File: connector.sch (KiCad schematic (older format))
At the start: 1 part, among them J11 DB15_Female_HighDensity_Mount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

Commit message: Added connector
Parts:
- removed J11: DB15_Female_HighDensity_MountingHoles, symbol Connector:DB15_Female_HighDensity_MountingHoles
- added J11: Conn_02x05_Counter_Clockwise, Connector_IDC:IDC-Header_2x05_P2.54mm_Vertical, symbol Connector_Generic:Conn_02x05_Counter_Clockwise
- added J12: DB9_Male_MountingHoles, symbol Connector:DB9_Male_MountingHoles
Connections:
- net labels removed: +10V
- wire segments 33 -> 44
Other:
- note added: "TODO: FOOTPRINT ???\n"

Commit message: First layout
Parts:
- removed J12: DB9_Male_MountingHoles, symbol Connector:DB9_Male_MountingHoles
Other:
- note removed: "TODO: FOOTPRINT ???\n"
- moved on the sheet: J11

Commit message: Fixed connector
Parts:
- removed J11: Conn_02x05_Counter_Clockwise, Connector_IDC:IDC-Header_2x05_P2.54mm_Vertical, symbol Connector_Generic:Conn_02x05_Counter_Clockwise
- added J11: Conn_02x05_Odd_Even, Connector_IDC:IDC-Header_2x05_P2.54mm_Vertical, symbol Connector_Generic:Conn_02x05_Odd_Even
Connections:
- net +6V: now also J11.3 (Pin_3)
- net -5V: now also J11.2 (Pin_2)
- net GND: now also J11.1 (Pin_1), J11.9 (Pin_9)
- net PA_EN: now also J11.10 (Pin_10)
- net PDET: now also J11.8 (Pin_8)
- net SCL: now also J11.6 (Pin_6)
- net SDA: now also J11.4 (Pin_4)
- net SW_CTR1: now also J11.5 (Pin_5)
- net SW_CTR2: now also J11.7 (Pin_7)
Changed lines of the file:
@@
 Comment4 ""
 $EndDescr
+Text HLabel 6300 4450 2    50   Output ~ 0
+PA_EN
 Text HLabel 5250 4250 0    50   Output ~ 0
-PA_EN
+SW_CTR1
 Text HLabel 5250 4350 0    50   Output ~ 0
-SW_CTR1
-Text HLabel 5250 4450 0    50   Output ~ 0
 SW_CTR2
-Text HLabel 6300 4250 2    50   BiDi ~ 0
+Text HLabel 6300 4150 2    50   BiDi ~ 0
 SDA
-Text HLabel 6300 4350 2    50   Output ~ 0
+Text HLabel 6300 4250 2    50   Output ~ 0
 SCL
-Text HLabel 6300 4450 2    50   Input ~ 0
+Text HLabel 6300 4350 2    50   Input ~ 0
 PDET
 $Comp
 L power:GND #PWR0109
 U 1 1 606566FC
-P 5350 2350
-F 0 "#PWR0109" H 5350 2100 50  0001 C CNN
-F 1 "GND" H 5355 2177 50  0000 C CNN
-F 2 "" H 5350 2350 50  0001 C CNN
-F 3 "" H 5350 2350 50  0001 C CNN
-	1    5350 2350
+P 5350 3100
+F 0 "#PWR0109" H 5350 2850 50  0001 C CNN
+F 1 "GND" H 5355 2927 50  0000 C CNN
+F 2 "" H 5350 3100 50  0001 C CNN
+F 3 "" H 5350 3100 50  0001 C CNN
+	1    5350 3100
 	1    0    0    -1
 $EndComp
@@
 L power:PWR_FLAG #FLG0101
 U 1 1 60656A1B
-P 5350 2250
-F 0 "#FLG0101" H 5350 2325 50  0001 C CNN
-F 1 "PWR_FLAG" H 5350 2423 50  0000 C CNN
-F 2 "" H 5350 2250 50  0001 C CNN
-F 3 "~" H 5350 2250 50  0001 C CNN
-	1    5350 2250
+P 5350 3000
+F 0 "#FLG0101" H 5350 3075 50  0001 C CNN
+F 1 "PWR_FLAG" H 5350 3173 50  0000 C CNN
+F 2 "" H 5350 3000 50  0001 C CNN
+F 3 "~" H 5350 3000 50  0001 C CNN
+	1    5350 3000
 	1    0    0    -1
 $EndComp
 Wire Wire Line
-	5350 2250 5350 2350
+	5350 3000 5350 3100
 $Comp
 L power:-5V #PWR0110
 U 1 1 60656FB7
-P 5750 2350
-F 0 "#PWR0110" H 5750 2450 50  0001 C CNN
-F 1 "-5V" H 5765 2523 50  0000 C CNN
-F 2 "" H 5750 2350 50  0001 C CNN
-F 3 "" H 5750 2350 50  0001 C CNN
-	1    5750 2350
+P 5750 3100
+F 0 "#PWR0110" H 5750 3200 50  0001 C CNN
+F 1 "-5V" H 5765 3273 50  0000 C CNN
+F 2 "" H 5750 3100 50  0001 C CNN
+F 3 "" H 5750 3100 50  0001 C CNN
+	1    5750 3100
 	-1   0    0    1
 $EndComp
@@
 L power:PWR_FLAG #FLG0102
 U 1 1 60657391
-P 5750 2250
-F 0 "#FLG0102" H 5750 2325 50  0001 C CNN
-F 1 "PWR_FLAG" H 5750 2423 50  0000 C CNN
-F 2 "" H 5750 2250 50  0001 C CNN
-F 3 "~" H 5750 2250 50  0001 C CNN
-	1    5750 2250
+P 5750 3000
+F 0 "#FLG0102" H 5750 3075 50  0001 C CNN
+F 1 "PWR_FLAG" H 5750 3173 50  0000 C CNN
+F 2 "" H 5750 3000 50  0001 C CNN
+F 3 "~" H 5750 3000 50  0001 C CNN
+	1    5750 3000
 	1    0    0    -1
 $EndComp
 Wire Wire Line
-	5750 2250 5750 2350
+	5750 3000 5750 3100
 $Comp
 L power:+6V #PWR0111
 U 1 1 60657FE5
-P 6250 2400
-F 0 "#PWR0111" H 6250 2250 50  0001 C CNN
-F 1 "+6V" H 6265 2573 50  0000 C CNN
-F 2 "" H 6250 2400 50  0001 C CNN
-F 3 "" H 6250 2400 50  0001 C CNN
-	1    6250 2400
+P 6250 3150
+F 0 "#PWR0111" H 6250 3000 50  0001 C CNN
+F 1 "+6V" H 6265 3323 50  0000 C CNN
+F 2 "" H 6250 3150 50  0001 C CNN
+F 3 "" H 6250 3150 50  0001 C CNN
+	1    6250 3150
 	1    0    0    -1
 $EndComp
@@
 L power:PWR_FLAG #FLG0103
 U 1 1 60658429
-P 6150 2250
-F 0 "#FLG0103" H 6150 2325 50  0001 C CNN
-F 1 "PWR_FLAG" H 6150 2423 50  0000 C CNN
-F 2 "" H 6150 2250 50  0001 C CNN
-F 3 "~" H 6150 2250 50  0001 C CNN
-	1    6150 2250
+P 6150 3000
+F 0 "#FLG0103" H 6150 3075 50  0001 C CNN
+F 1 "PWR_FLAG" H 6150 3173 50  0000 C CNN
+F 2 "" H 6150 3000 50  0001 C CNN
+F 3 "~" H 6150 3000 50  0001 C CNN
+	1    6150 3000
 	1    0    0    -1
 $EndComp
 Wire Wire Line
-	6150 2250 6150 2450
+	6150 3000 6150 3200
 Wire Wire Line
-	6150 2450 6250 2450
+	6150 3200 6250 3200
 Wire Wire Line
-	6250 2450 6250 2400
-$Comp
-L Connector_Generic:Conn_02x05_Counter_Clockwise J11
-U 1 1 606A85A2
-P 5700 4250
-F 0 "J11" H 5750 3950 50  0000 C CNN
-F 1 "Conn_02x05_Counter_Clockwise" H 5750 3700 50  0000 C CNN
-F 2 "Connector_IDC:IDC-Header_2x05_P2.54mm_Vertical" H 5700 4250 50  0001 C CNN
-F 3 "~" H 5700 4250 50  0001 C CNN
-	1    5700 4250
-	1    0    0    -1
-$EndComp
+	6250 3200 6250 3150
+Wire Wire Line
+	6000 4250 6300 4250
 Wire Wire Line
 	6000 4350 6300 4350
-Wire Wire Line
-	6000 4450 6300 4450
 $Comp
 L power:+6V #PWR0107
 U 1 1 606E1715
-P 5400 3950
-F 0 "#PWR0107" H 5400 3800 50  0001 C CNN
-F 1 "+6V" H 5415 4123 50  0000 C CNN
-F 2 "" H 5400 3950 50  0001 C CNN
-F 3 "" H 5400 3950 50  0001 C CNN
-	1    5400 3950
+P 5300 3950
+F 0 "#PWR0107" H 5300 3800 50  0001 C CNN
+F 1 "+6V" H 5315 4123 50  0000 C CNN
+F 2 "" H 5300 3950 50  0001 C CNN
+F 3 "" H 5300 3950 50  0001 C CNN
+	1    5300 3950
 	1    0    0    -1
 $EndComp
-Wire Wire Line
-	5400 3950 5400 4050
-Wire Wire Line
-	5400 4050 5500 4050
 $Comp
 L power:GND #PWR0108
@@
 	1    0    0    -1
 $EndComp
-Wire Wire Line
-	5400 4550 5400 4150
-Wire Wire Line
-	5400 4150 5500 4150
 $Comp
 L power:-5V #PWR0112
 U 1 1 606E3CEE
-P 6200 4550
-F 0 "#PWR0112" H 6200 4650 50  0001 C CNN
-F 1 "-5V" H 6200 4700 50  0000 C CNN
-F 2 "" H 6200 4550 50  0001 C CNN
-F 3 "" H 6200 4550 50  0001 C CNN
-	1    6200 4550
-	-1   0    0    1
-$EndComp
-$Comp
-L power:GND #PWR0113
-U 1 1 606E4A32
 P 6100 4550
-F 0 "#PWR0113" H 6100 4300 50  0001 C CNN
-F 1 "GND" H 6050 4400 50  0000 C CNN
+F 0 "#PWR0112" H 6100 4650 50  0001 C CNN
+F 1 "-5V" H 6100 4700 50  0000 C CNN
 F 2 "" H 6100 4550 50  0001 C CNN
 F 3 "" H 6100 4550 50  0001 C CNN
 	1    6100 4550
-	1    0    0    -1
+	-1   0    0    1
 $EndComp
-Wire Wire Line
-	6100 4550 6100 4150
-Wire Wire Line
-	6100 4150 6000 4150
-Wire Wire Line
-	6200 4550 6200 4050
-Wire Wire Line
-	6200 4050 6000 4050
 Wire Wire Line
 	5250 4250 5500 4250
@@
 	5250 4350 5500 4350
 Wire Wire Line
-	5250 4450 5500 4450
+	6300 4450 6000 4450
 Wire Wire Line
-	6000 4250 6300 4250
+	6000 4150 6300 4150
+Wire Wire Line
+	5400 4050 5500 4050
+Wire Wire Line
+	5400 4050 5400 4450
+Wire Wire Line
+	5300 3950 5300 4150
+$Comp
+L Connector_Generic:Conn_02x05_Odd_Even J11
+U 1 1 6067C933
+P 5700 4250
+F 0 "J11" H 5750 3750 50  0000 C CNN
+F 1 "Conn_02x05_Odd_Even" H 5750 3650 50  0000 C CNN
+F 2 "Connector_IDC:IDC-Header_2x05_P2.54mm_Vertical" H 5700 4250 50  0001 C CNN
+F 3 "~" H 5700 4250 50  0001 C CNN
+	1    5700 4250
+	1    0    0    -1
+$EndComp
+Wire Wire Line
+	5300 4150 5500 4150
+Wire Wire Line
+	5500 4450 5400 4450
+Connection ~ 5400 4450
+Wire Wire Line
+	5400 4450 5400 4550
+Wire Wire Line
+	6100 4050 6100 4550
+Wire Wire Line
+	6100 4050 6000 4050
 $EndSCHEMATC

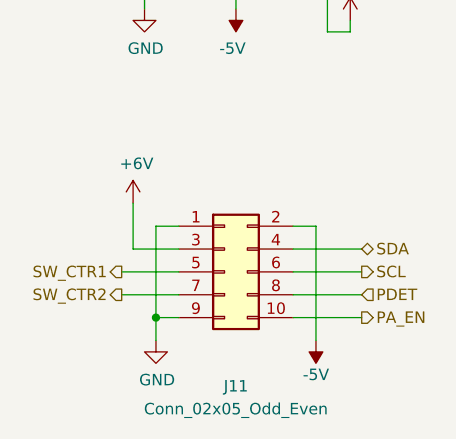
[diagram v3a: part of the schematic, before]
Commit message: Added RX shield
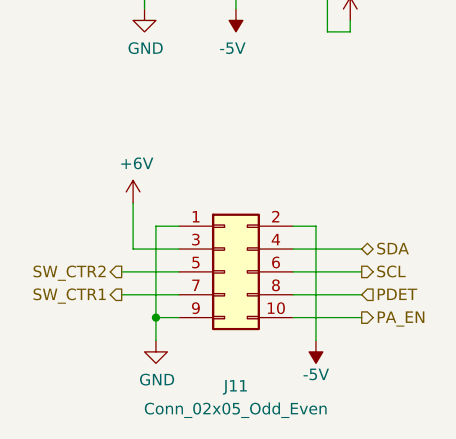
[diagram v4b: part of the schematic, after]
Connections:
- net SW_CTR1: now also J11.7 (Pin_7); no longer J11.5 (Pin_5)
- net SW_CTR2: now also J11.5 (Pin_5); no longer J11.7 (Pin_7)
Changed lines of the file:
@@
 Text HLabel 6300 4450 2    50   Output ~ 0
 PA_EN
+Text HLabel 5250 4350 0    50   Output ~ 0
+SW_CTR1
 Text HLabel 5250 4250 0    50   Output ~ 0
-SW_CTR1
-Text HLabel 5250 4350 0    50   Output ~ 0
 SW_CTR2
 Text HLabel 6300 4150 2    50   BiDi ~ 0
